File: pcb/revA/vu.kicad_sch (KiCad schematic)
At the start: 32 parts

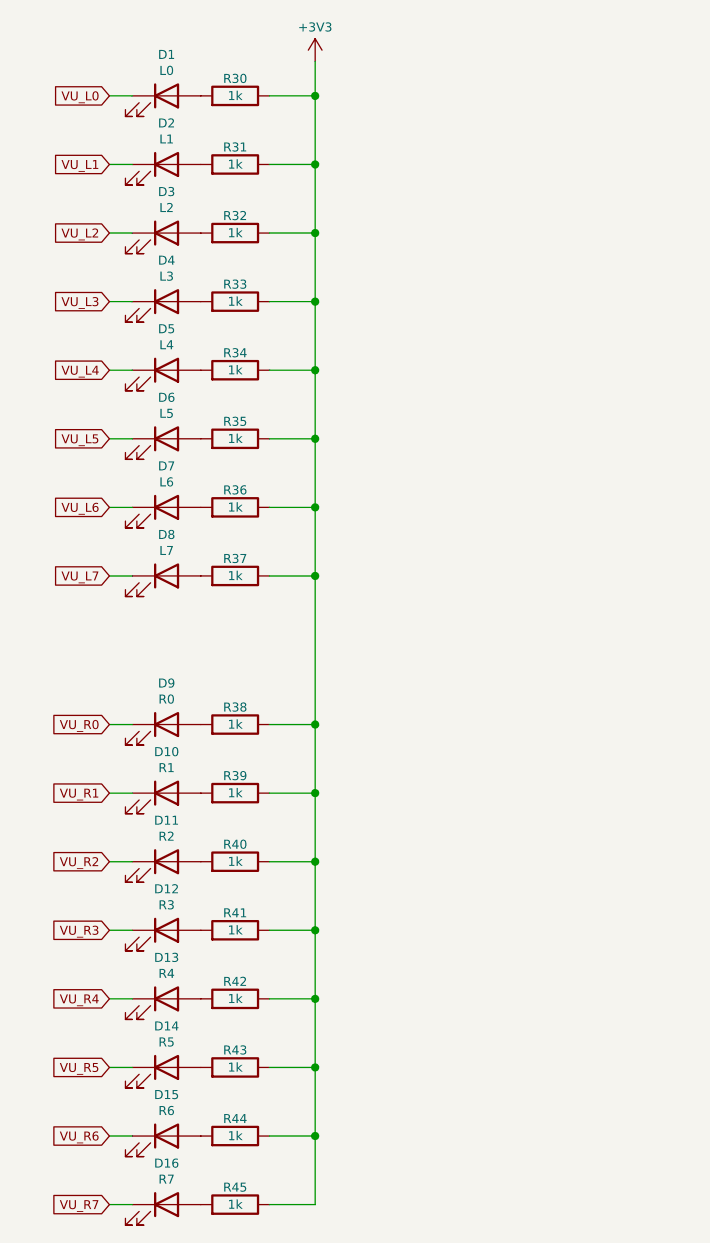
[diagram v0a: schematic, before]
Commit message: Updated gerbers to min 0.2/0.45 vias, firmware build for xc6slx16
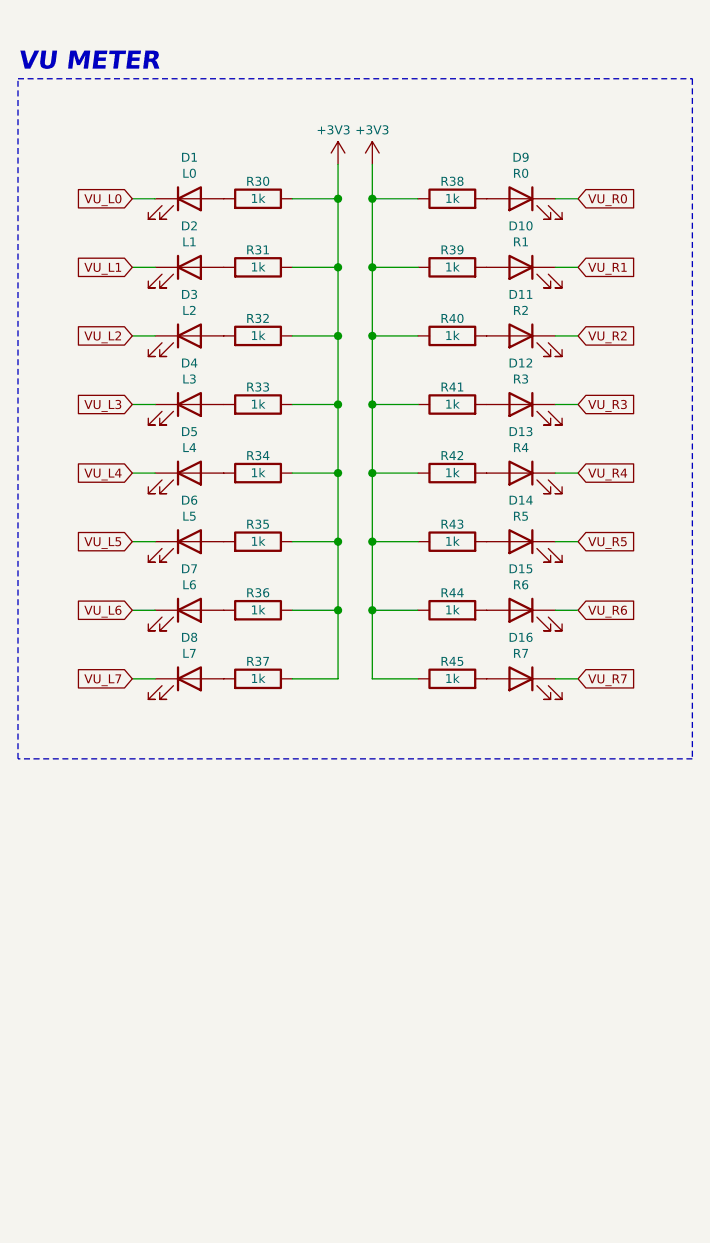
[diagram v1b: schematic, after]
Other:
- note added: "VU METER"
- moved on the sheet: D1, D10, D11, D12, D13, D14, D15, D16, D2, D3, D4, D5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

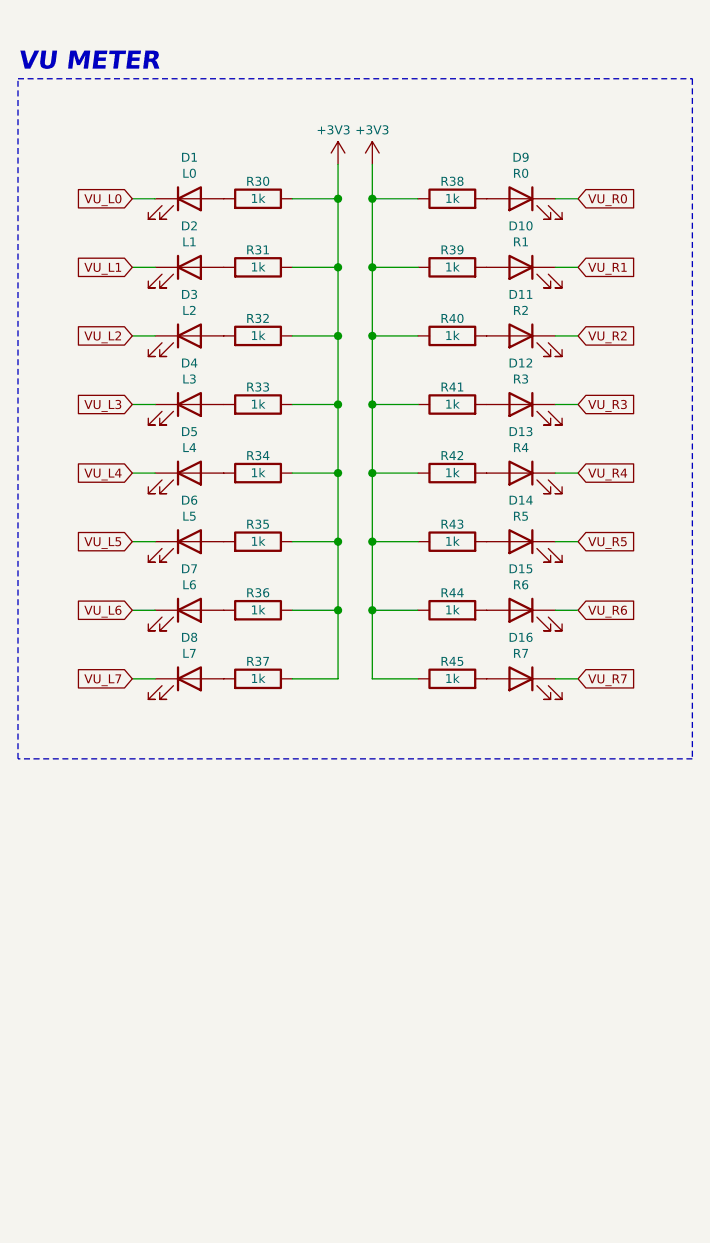
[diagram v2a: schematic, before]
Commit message: Updated revA (cosmetic changes)
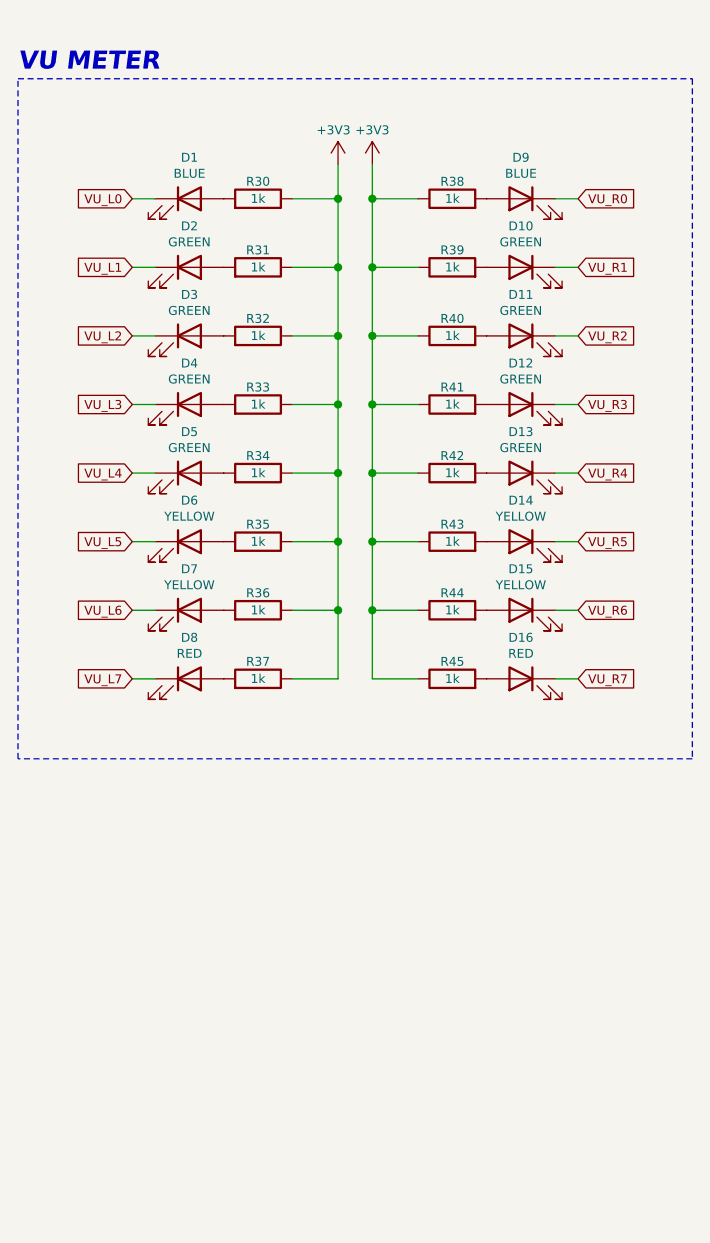
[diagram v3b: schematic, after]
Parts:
- D1: value L0 -> BLUE
- D10: value R1 -> GREEN
- D11: value R2 -> GREEN
- D12: value R3 -> GREEN
- D13: value R4 -> GREEN
- D14: value R5 -> YELLOW
- D15: value R6 -> YELLOW
- D16: value R7 -> RED
- D2: value L1 -> GREEN
- D3: value L2 -> GREEN
- D4: value L3 -> GREEN
- D5: value L4 -> GREEN
- D6: value L5 -> YELLOW
- D7: value L6 -> YELLOW
- D8: value L7 -> RED
- D9: value R0 -> BLUE
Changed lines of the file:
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@@
 			)
 		)
-		(property "Value" "L1"
+		(property "Value" "GREEN"
 			(at 52.07 42.926 0)
 			(show_name no)
@@
 			)
 		)
-		(property "Value" "R6"
+		(property "Value" "YELLOW"
 			(at 88.9 81.026 0)
 			(show_name no)
@@
 			)
 		)
-		(property "Value" "L0"
+		(property "Value" "BLUE"
 			(at 52.07 35.306 0)
 			(show_name no)
@@
 			)
 		)
-		(property "Value" "L6"
+		(property "Value" "YELLOW"
 			(at 52.07 81.026 0)
 			(show_name no)
@@
 			)
 		)
-		(property "Value" "L4"
+		(property "Value" "GREEN"
 			(at 52.07 65.786 0)
 			(show_name no)
@@
 			)
 		)
-		(property "Value" "R3"
+		(property "Value" "GREEN"
 			(at 88.9 58.166 0)
 			(show_name no)
@@
 			)
 		)
-		(property "Value" "L2"
+		(property "Value" "GREEN"
 			(at 52.07 50.546 0)
 			(show_name no)
@@
 			)
 		)
-		(property "Value" "R2"
+		(property "Value" "GREEN"
 			(at 88.9 50.546 0)
 			(show_name no)
@@
 			)
 		)
-		(property "Value" "L7"
+		(property "Value" "RED"
 			(at 52.07 88.646 0)
 			(show_name no)
@@
 			)
 		)
-		(property "Value" "R5"
+		(property "Value" "YELLOW"
 			(at 88.9 73.406 0)
 			(show_name no)
@@
 			)
 		)
-		(property "Value" "R4"
+		(property "Value" "GREEN"
 			(at 88.9 65.786 0)
 			(show_name no)
@@
 			)
 		)
-		(property "Value" "R7"
+		(property "Value" "RED"
 			(at 88.9 88.646 0)
 			(show_name no)
@@
 			)
 		)
-		(property "Value" "R1"
+		(property "Value" "GREEN"
 			(at 88.9 42.926 0)
 			(show_name no)
@@
 			)
 		)
-		(property "Value" "R0"
+		(property "Value" "BLUE"
 			(at 88.9 35.306 0)
 			(show_name no)
@@
 			)
 		)
-		(property "Value" "L5"
+		(property "Value" "YELLOW"
 			(at 52.07 73.406 0)
 			(show_name no)
@@
 			)
 		)
-		(property "Value" "L3"
+		(property "Value" "GREEN"
 			(at 52.07 58.166 0)
 			(show_name no)
